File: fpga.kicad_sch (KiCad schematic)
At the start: 1 part, among them U2 LFE5UM5G-85F-8BG381x

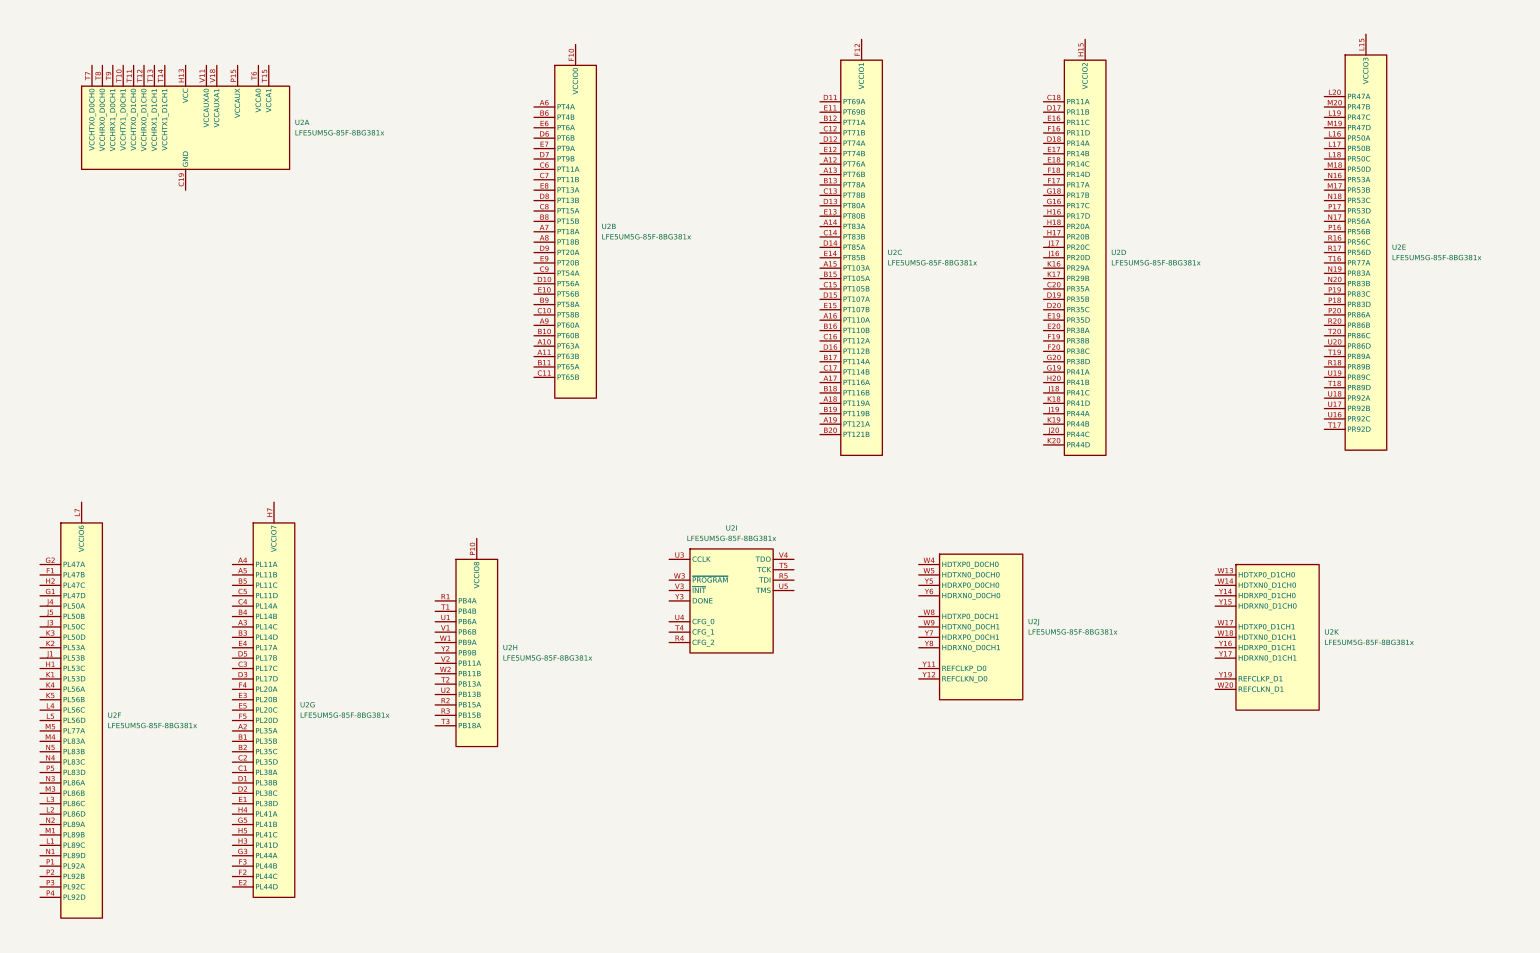
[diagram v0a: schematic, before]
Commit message: Adicionando novos datasheets e comecando power
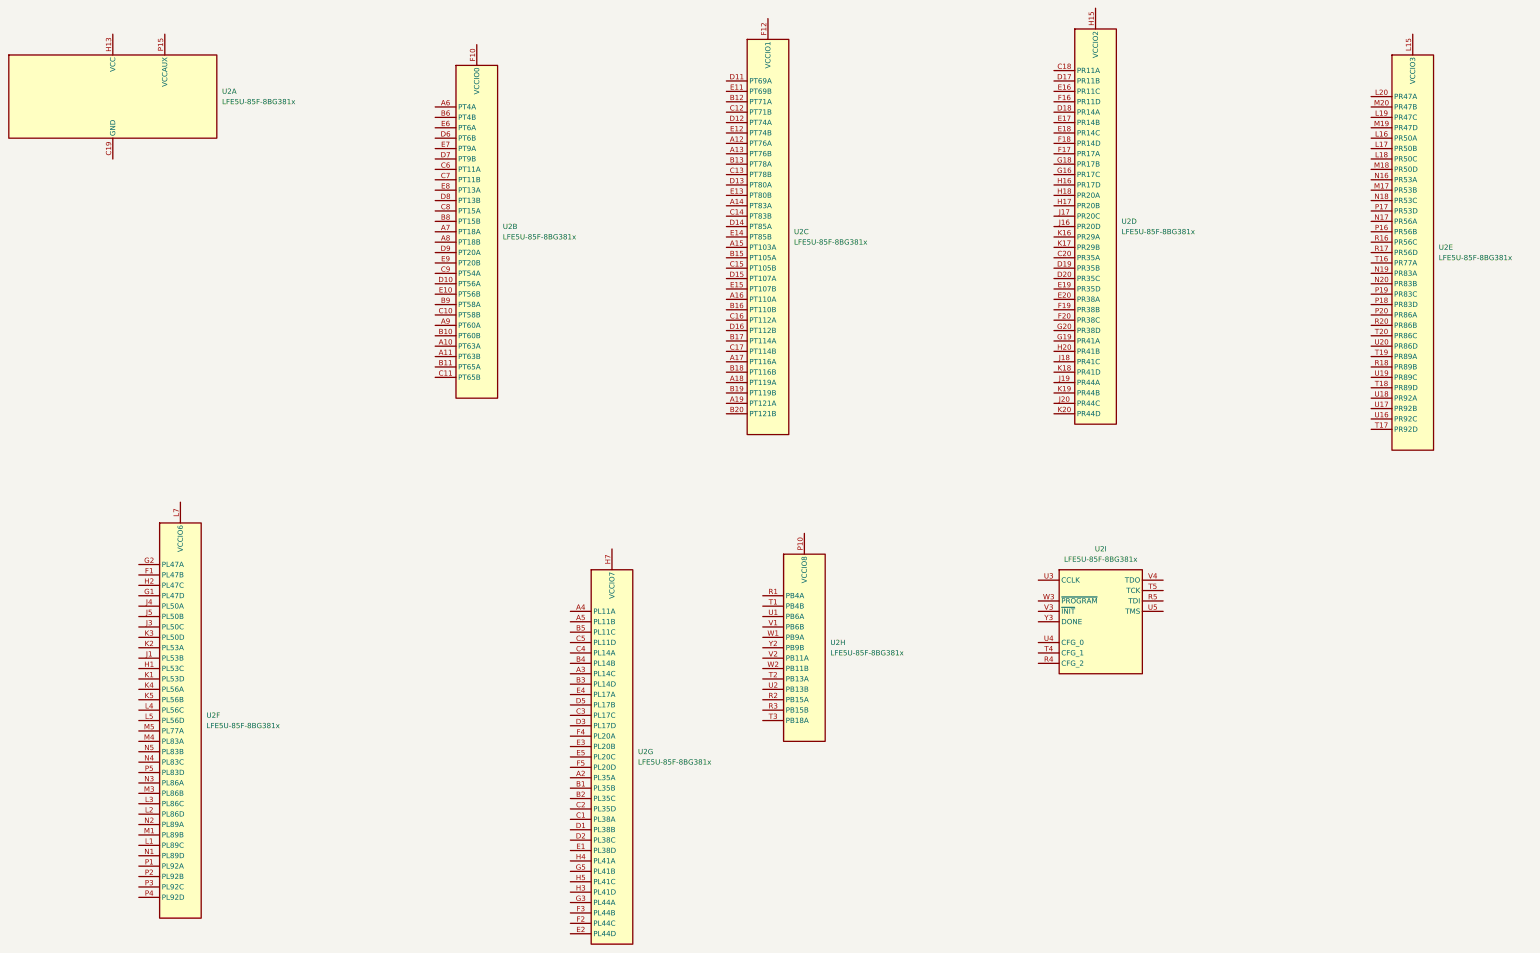
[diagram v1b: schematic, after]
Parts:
- removed U2: LFE5UM5G-85F-8BG381x, Package_BGA:Lattice_caBGA-381_17.0x17.0mm_Layout20x20_P0.8mm_Ball0.4mm_Pad0.4mm_NSMD, symbol FPGA_Lattice:LFE5UM5G-85F-8BG381x
- added U2: LFE5U-85F-8BG381x, Package_BGA:Lattice_caBGA-381_17.0x17.0mm_Layout20x20_P0.8mm_Ball0.4mm_Pad0.4mm_NSMD, symbol FPGA_Lattice:LFE5U-85F-8BG381x
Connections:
- new net: U2.L14 (VCCIO3), U2.L15 (VCCIO3), U2.M15 (VCCIO3)
- new net: U2.B14 (GND), U2.B7 (GND), U2.C19 (GND), U2.D4 (GND), U2.F13 (GND), U2.F14 (GND), U2.F7 (GND), U2.F8 (GND), U2.G10 (GND), U2.G11 (GND), U2.G12 (GND), U2.G13 (GND), U2.G14 (GND), U2.G15 (GND), U2.G17 (GND), U2.G4 (GND), U2.G6 (GND), U2.G7 (GND), U2.G8 (GND), U2.G9 (GND), U2.H19 (GND), U2.J10 (GND), U2.J11 (GND), U2.J12 (GND), U2.J14 (GND), U2.J2 (GND), U2.J7 (GND), U2.J9 (GND), U2.K10 (GND), U2.K11 (GND), U2.K12 (GND), U2.K14 (GND), U2.K15 (GND), U2.K6 (GND), U2.K7 (GND), U2.K9 (GND), U2.L10 (GND), U2.L11 (GND), U2.L12 (GND), U2.L9 (GND), U2.M10 (GND), U2.M11 (GND), U2.M12 (GND), U2.M14 (GND), U2.M16 (GND), U2.M2 (GND), U2.M7 (GND), U2.M9 (GND), U2.N14 (GND), U2.N15 (GND), U2.N6 (GND), U2.N7 (GND), U2.P11 (GND), U2.P12 (GND), U2.P13 (GND), U2.P14 (GND), U2.P7 (GND), U2.P8 (GND), U2.R19 (GND), U2.T10 (GND), U2.T11 (GND), U2.T12 (GND), U2.T13 (GND), U2.T14 (GND), U2.T15 (GND), U2.T6 (GND), U2.T7 (GND), U2.T8 (GND), U2.T9 (GND), U2.U10 (GND), U2.U11 (GND), U2.U12 (GND), U2.U13 (GND), U2.U14 (GND), U2.U15 (GND), U2.U6 (GND), U2.U7 (GND), U2.U8 (GND), U2.U9 (GND), U2.V10 (GND), U2.V11 (GND), U2.V12 (GND), U2.V13 (GND), U2.V14 (GND), U2.V15 (GND), U2.V16 (GND), U2.V17 (GND), U2.V18 (GND), U2.V19 (GND), U2.V20 (GND), U2.V5 (GND), U2.V6 (GND), U2.V7 (GND), U2.V8 (GND), U2.V9 (GND), U2.W12 (GND), U2.W15 (GND), U2.W16 (GND), U2.W19 (GND), U2.W20 (GND), U2.W6 (GND), U2.W7 (GND), U2.Y11 (GND), U2.Y12 (GND), U2.Y14 (GND), U2.Y15 (GND), U2.Y16 (GND), U2.Y17 (GND), U2.Y19 (GND), U2.Y5 (GND), U2.Y6 (GND), U2.Y7 (GND), U2.Y8 (GND)
- new net: U2.F15 (VCCAUX), U2.F6 (VCCAUX), U2.P15 (VCCAUX), U2.P6 (VCCAUX)
- new net: U2.H10 (VCC), U2.H11 (VCC), U2.H12 (VCC), U2.H13 (VCC), U2.H8 (VCC), U2.H9 (VCC), U2.J13 (VCC), U2.J8 (VCC), U2.K13 (VCC), U2.K8 (VCC), U2.L13 (VCC), U2.L8 (VCC), U2.M13 (VCC), U2.M8 (VCC), U2.N10 (VCC), U2.N11 (VCC), U2.N12 (VCC), U2.N13 (VCC), U2.N8 (VCC), U2.N9 (VCC)
- new net: U2.P10 (VCCIO8), U2.P9 (VCCIO8)
- new net: U2.L6 (VCCIO6), U2.L7 (VCCIO6), U2.M6 (VCCIO6)
- new net: U2.F10 (VCCIO0), U2.F9 (VCCIO0)
- new net: U2.H6 (VCCIO7), U2.H7 (VCCIO7), U2.J6 (VCCIO7)
- new net: U2.F11 (VCCIO1), U2.F12 (VCCIO1)
- new net: U2.H14 (VCCIO2), U2.H15 (VCCIO2), U2.J15 (VCCIO2)
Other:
- title: ECP5 85F Platonic Board -> PatchLogic 85 FPGA Board

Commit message: Implementando power e ligando jtag e flash a fpga
Implementando circuito de power. Ligando JTAG e memoria FLASH quad SPI a
FPGA. Iniciando implementacão da DRAM e outros modulos
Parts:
- added C54: 100n, symbol Device:C_Small
- added C55: 100n, symbol Device:C
- added D12: BLUE, symbol Device:LED
- added D13: RED, symbol Device:LED
- added D14: GREEN, symbol Device:LED
- added J15: Flash, Connector_PinHeader_2.54mm:PinHeader_2x04_P2.54mm_Vertical, symbol Connector_Generic:Conn_02x04_Odd_Even
- added J16: JTAG, Connector_PinSocket_2.54mm:PinSocket_1x06_P2.54mm_Vertical, symbol Connector_Generic:Conn_01x06
- added Q1: 2N7002, Package_TO_SOT_SMD:SOT-23, symbol Transistor_FET:2N7002
- added R10: R, symbol Device:R
- added R12: 22R, symbol Device:R
- added R38, R41, R42: 10k, symbol Device:R
- added R39, R40: 1K, symbol Device:R
- added R43: 470R, symbol Device:R
- added R44, R45, R46, R47, R48, R49, R9: 1k, symbol Device:R
- added RN6: 4.7k, Resistor_SMD:R_Array_Convex_4x0603, symbol Device:R_Pack04
- added RN7: 10k, symbol Device:R_Pack04
- added SW11: SW_Push, symbol Switch:SW_Push
- added U18: W25Q128JVS, Package_SO:SOIC-8_5.23x5.23mm_P1.27mm, symbol Memory_Flash:W25Q128JVS
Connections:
- net FPGA_CFG_2: now reaches U2.R4 (CFG_2)
- net FPGA_CFG_2: now also R46.2, R49.1
- net JTAG_TDO: now reaches U2.R5 (TDI)
- net JTAG_TDO: now also J16.4 (Pin_4), RN6.3 (R3.1)
- net FPGA_CFG_1: now reaches U2.T4 (CFG_1)
- net FPGA_CFG_1: now also R45.2, R48.1
- net JTAG_TDI: now reaches U2.T5 (TCK)
- net JTAG_TDI: now also J16.3 (Pin_3), RN6.2 (R2.1)
- net FPGA_CFG_0: now reaches U2.U4 (CFG_0)
- net FPGA_CFG_0: now also R44.2, R47.1
- net JTAG_TMS: now reaches U2.U5 (TMS)
- net JTAG_TMS: now also J16.5 (Pin_5)
- net FPGA_INITN: now reaches U2.V3 (~{INIT})
- net FPGA_INITN: now also D13.1 (K), R41.2
- net JTAG_TCK: now reaches U2.V4 (TDO)
- net JTAG_TCK: now also J16.2 (Pin_2), RN6.1 (R1.1)
- net FPGA_PROGRAMN: now reaches U2.W3 (~{PROGRAM})
- net FPGA_PROGRAMN: now also C54.1, D12.1 (K), R38.2, SW11.2
- net FPGA_DONE: now reaches U2.Y3 (DONE)
- net FPGA_DONE: now also Q1.1 (G), R42.2
- net SD_D0: now reaches U2.R1 (PB4A)
- net FLASH_CSN: now reaches U2.R2 (PB15A)
- net FLASH_CSN: now also J15.3 (Pin_3), R10.2, U18.1 (~{CS})
- net at U2.R3 (PB15B): now also R12.1
- net SD_D2: now reaches U2.T1 (PB4B)
- net SD_D1: now reaches U2.U1 (PB6A)
- net SD_CMD: now reaches U2.U2 (PB13B)
- net SD_D3: now reaches U2.V1 (PB6B)
- net FLASH_D1: now reaches U2.V2 (PB11A)
- net FLASH_D1: now also J15.4 (Pin_4), RN7.2 (R2.1), U18.2 (DO(IO1))
- net FLASH_D3: now reaches U2.W1 (PB9A)
- net FLASH_D3: now also J15.8 (Pin_8), RN7.4 (R4.1), U18.7 (IO3)
- net FLASH_D0: now reaches U2.W2 (PB11B)
- net FLASH_D0: now also J15.2 (Pin_2), RN7.1 (R1.1), U18.5 (DI(IO0))
- net FLASH_D2: now reaches U2.Y2 (PB9B)
- net FLASH_D2: now also J15.6 (Pin_6), RN7.3 (R3.1), U18.3 (IO2)
- net FPGA_SYS_CLK: now reaches U2.J19 (PR44A)
- new net: D14.2 (A), R43.1
- new net: D14.1 (K), Q1.3 (D)
- new net: D12.2 (A), R39.1
- new net: D13.2 (A), R40.2
- new net +3V3: C55.1, J15.1 (Pin_1), J16.1 (Pin_1), R10.1, R38.1, R39.2, R40.1, R41.1, R42.1, R43.2, R44.1, R45.1, R46.1, R9.1, RN6.6 (R3.2), RN6.7 (R2.2), RN6.8 (R1.2), RN7.5 (R4.2), RN7.6 (R3.2), RN7.7 (R2.2), RN7.8 (R1.2), U18.8 (VCC)
- new net FLASH_CLK: J15.5 (Pin_5), R9.2, U18.6 (CLK)
- new net GND: C54.2, C55.2, J15.7 (Pin_7), J16.6 (Pin_6), Q1.2 (S), R47.2, R48.2, R49.2, SW11.1, U18.4 (GND)
- new net SD_CLK: R12.2
- no-connect marks 0 -> 2
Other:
- moved on the sheet: U2B, U2C, U2H, U2I
